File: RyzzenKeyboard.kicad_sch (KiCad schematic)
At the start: 16 parts, among them SW1 SW_SPDT, U100 STM32F411CEUx, Y1 25MHz

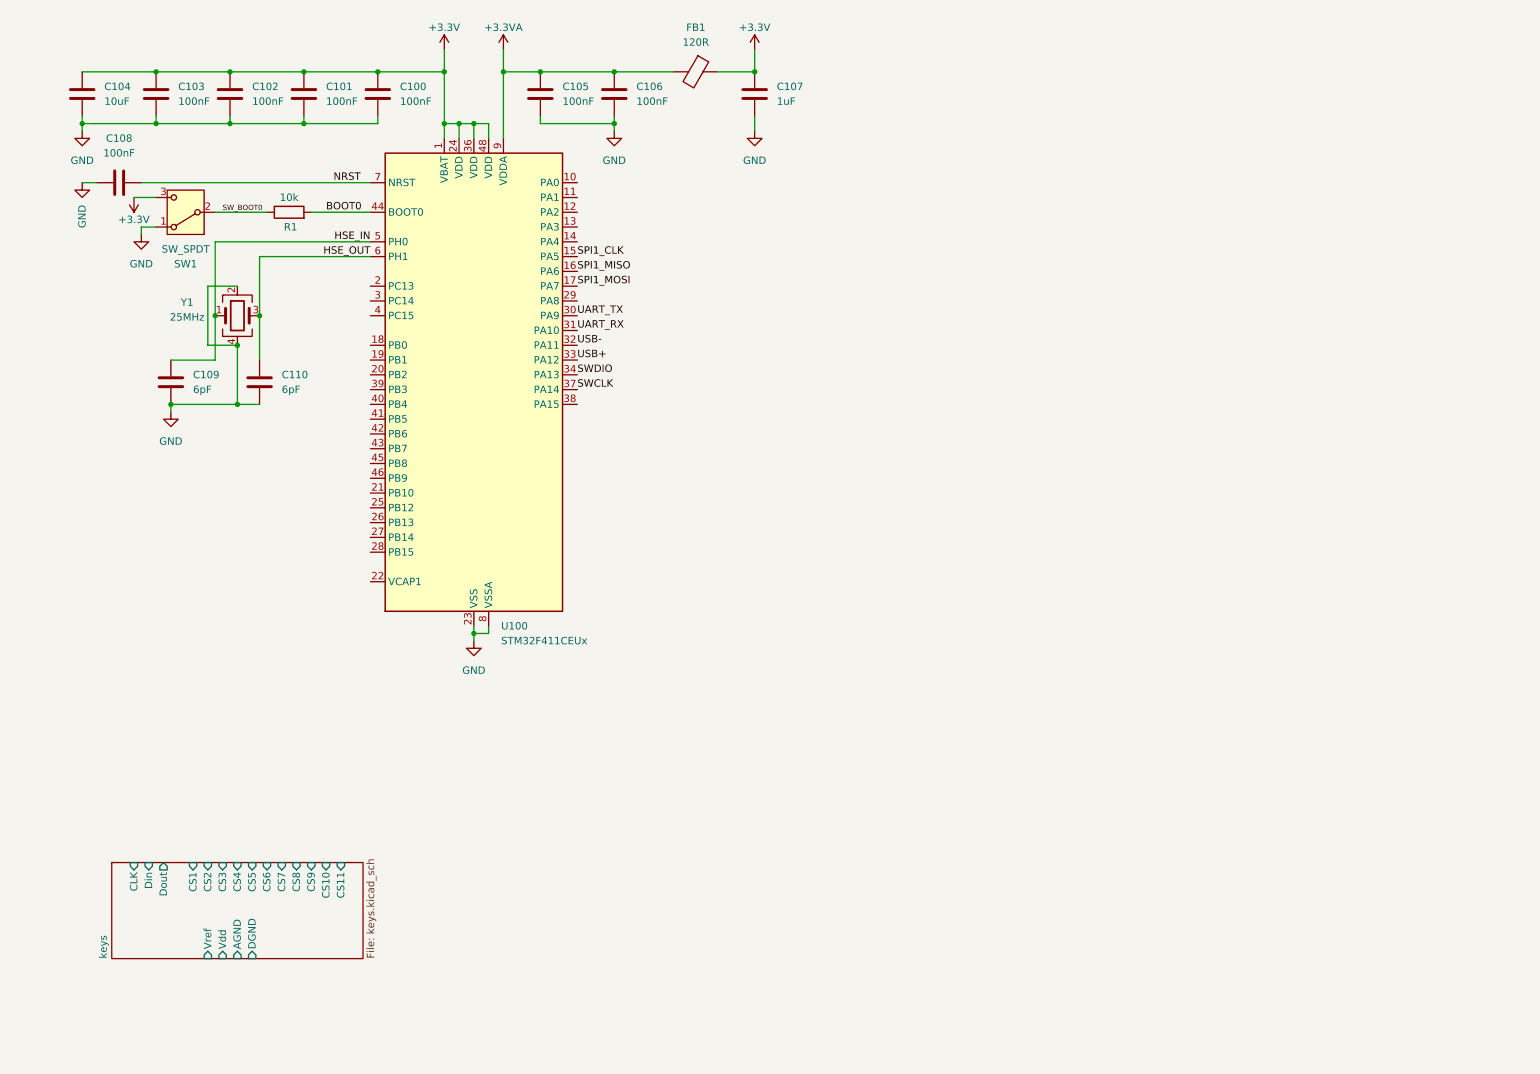
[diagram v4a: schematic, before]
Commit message: [UPDATE](TMR) switched to TMR sensors + added ldo
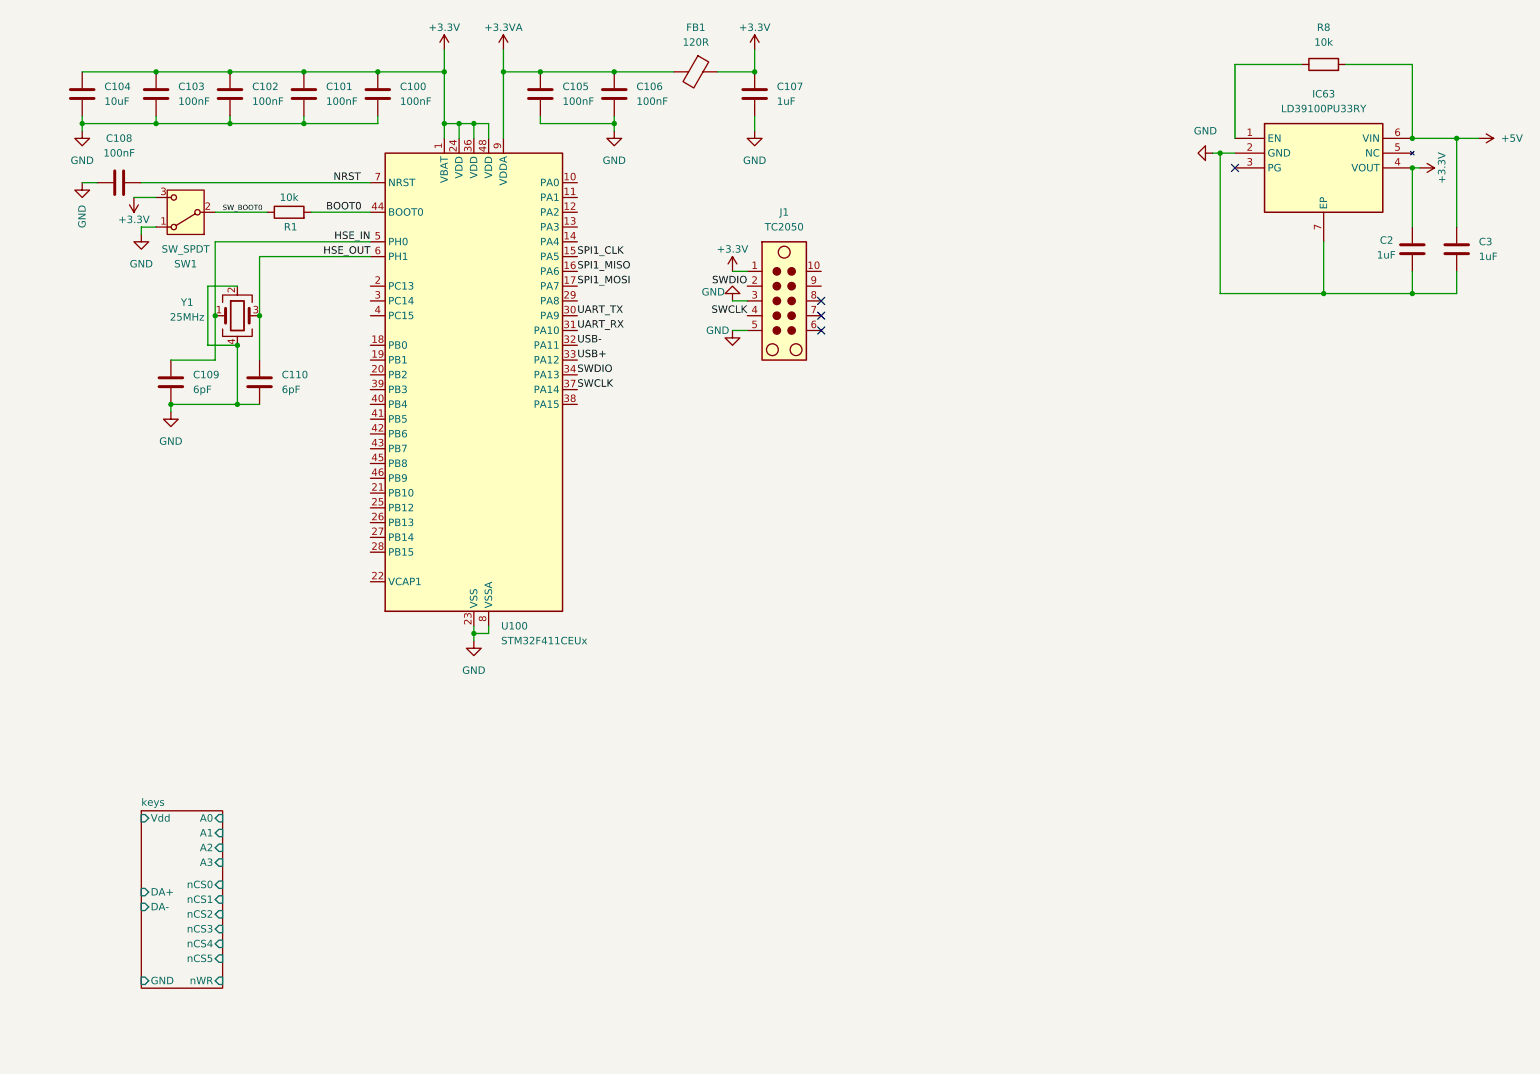
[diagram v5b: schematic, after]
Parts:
- added C2, C3: 1uF, symbol Device:C
- added IC63: LD39100PU33RY, SON95P300X300X90-7N-D, symbol LD39100PU33RY:LD39100PU33RY
- added J1: TC2050, Connector:Tag-Connect_TC2050-IDC-NL_2x05_P1.27mm_Vertical, symbol Connector:TC2050
- added R8: 10k, symbol Device:R
- Y1: footprint (none) -> ECS-250-8-30B-CKM:XTAL_ECS-250-8-30B-CKM
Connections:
- net +3.3V: now also C2.1, IC63.4 (VOUT), J1.1
- net GND: now also C2.2, C3.2, IC63.2 (GND), IC63.7 (EP), J1.3, J1.5
- net SWCLK: now also J1.4
- net SWDIO: now also J1.2
- new net: IC63.1 (EN), R8.1
- new net +5V: C3.1, IC63.6 (VIN), R8.2
- no-connect marks 0 -> 4
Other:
- sheet keys ports: added A0, A1, A2, A3, DA+, DA-, GND, nCS0, nCS1, nCS2, nCS3, nCS4, nCS5, nWR; removed AGND, CLK, CS1, CS10, CS11, CS2, CS3, CS4, CS5, CS6, CS7, CS8, CS9, DGND, Din, Dout, Vref

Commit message: [ADD](HID SPI Bridge)
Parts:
- removed SW1: SW_SPDT, symbol Switch:SW_SPDT
- added D1: LED, symbol Device:LED
- added R9: 1k5, symbol Device:R
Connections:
- net SW_BOOT0 is gone; now on net GND: R1.1
- net GND: now also R9.2
- net at IC63.3 (PG): now also D1.2 (A)
- net +5V renamed VBUS
- new net: D1.1 (K), R9.1
- no-connect marks 4 -> 3
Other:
- added sheet HID_SPI_bridge (HID_SPI_bridge.kicad_sch)
- moved on the sheet: C2, C3, IC63, R8

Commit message: [ADD](General) v1
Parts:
- removed R9: 1k5, symbol Device:R
- added R3: 1k5, symbol Device:R
- renumbered C104 to C1, C106 to C10, C107 to C11, C2 to C12, C3 to C13, C103 to C2, C109 to C3, C108 to C4, C102 to C5, C110 to C6, C101 to C7, C100 to C8, C105 to C9, IC63 to IC1, R8 to R2, U100 to U1
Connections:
- net +3.3V: now also D1.2 (A)
- net GND: now also J1.9, R3.2
- net NRST: now also J1.10
- net UART_RX: now also J1.7
- net UART_TX: now also J1.8
- net at IC1.3 (PG): no longer D1.2 (A)
- net at D1.1 (K): now also R3.1
- net DA+: now reaches U1.10 (PA0)
- net DA-: now reaches U1.11 (PA1)
- net nWR: now reaches U1.13 (PA3)
- net A0: now reaches U1.18 (PB0)
- net A1: now reaches U1.19 (PB1)
- net A2: now reaches U1.20 (PB2)
- net A3: now reaches U1.21 (PB10)
- net CS_USB3: now reaches U1.25 (PB12)
- net CS_USB2: now reaches U1.26 (PB13)
- net CS_USB1: now reaches U1.27 (PB14)
- net nCS0: now reaches U1.39 (PB3)
- net nCS1: now reaches U1.40 (PB4)
- net nCS2: now reaches U1.41 (PB5)
- net nCS3: now reaches U1.42 (PB6)
- net nCS4: now reaches U1.43 (PB7)
- net nCS5: now reaches U1.45 (PB8)
- net USB+: no longer names the net of U1.33 (PA12)
- net USB-: no longer names the net of U1.32 (PA11)
- no-connect marks 3 -> 14
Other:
- added sheet HID_SPI_bridge1 (HID_SPI_bridge.kicad_sch)
- added sheet HID_SPI_bridge2 (HID_SPI_bridge.kicad_sch)
- sheet HID_SPI_bridge ports: added NRST, SPI_CS, SPI_MISO, SPI_MOSI, SPI_SCK, SWCLK, SWDIO; removed none
- note added: "Analog keys"
- note added: "Main microcontroller"
- note added: "Power supply"
- note added: "SPI to triple USB HID bridge"
- company: (none) -> Ryzzen
- title: (none) -> TMR based triple USB Keyboard
- moved on the sheet: C1, C10, C11, C12, C13, C2, C3, C4, C5, C6, C7, C8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

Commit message: [ADD](General) v2 split
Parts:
- added D37: D_Schottky, symbol Device:D_Schottky
- added J2, J3: Conn_01x16_Socket, symbol Connector:Conn_01x16_Socket
- added J4: USB_C_Receptacle_USB2.0_14P, symbol Connector:USB_C_Receptacle_USB2.0_14P
- added R10, R11: 5.1k, symbol Device:R
- added R4: 10k, symbol Device:R
- added U37: W25Q32JVSS, Package_SO:SOIC-8_5.3x5.3mm_P1.27mm, symbol Memory_Flash:W25Q32JVSS
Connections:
- net +3.3V: now also R4.1, U37.8 (VCC)
- net +3.3VA: now also J2.14 (Pin_14), J3.14 (Pin_14)
- net A0: now also J2.6 (Pin_6), J3.6 (Pin_6)
- net A1: now also J2.5 (Pin_5), J3.5 (Pin_5)
- net A2: now also J2.4 (Pin_4), J3.4 (Pin_4)
- net A3: now also J2.3 (Pin_3), J3.3 (Pin_3)
- net DA+: now also J2.12 (Pin_12), J3.12 (Pin_12)
- net DA-: now also J2.11 (Pin_11), J3.11 (Pin_11)
- net GND: now also J2.1 (Pin_1), J2.10 (Pin_10), J2.13 (Pin_13), J2.16 (Pin_16), J3.1 (Pin_1), J3.10 (Pin_10), J3.13 (Pin_13), J3.16 (Pin_16), J4.A1 (GND), J4.A12 (GND), J4.B1 (GND), J4.B12 (GND), R10.1, R11.1, U37.4 (GND)
- net SPI1_CLK: now also U37.6 (CLK)
- net SPI1_MISO: now also U37.2 (DO/IO_{1})
- net SPI1_MOSI: now also U37.5 (DI/IO_{0})
- net VBUS: now also D37.1 (K), J2.15 (Pin_15), J3.15 (Pin_15)
- net nCS0: now also J2.8 (Pin_8), J3.8 (Pin_8)
- net nCS1: now also J2.7 (Pin_7), J3.7 (Pin_7)
- net nWR: now also J2.9 (Pin_9), J3.9 (Pin_9)
- net nCS_FLASH: now reaches U1.28 (PB15)
- net nCS_FLASH: now also U37.1 (~{CS})
- net Din: now reaches U1.46 (PB9)
- net Din: now also J2.2 (Pin_2), J3.2 (Pin_2)
- new net: D37.2 (A), J4.A4 (VBUS), J4.A9 (VBUS), J4.B4 (VBUS), J4.B9 (VBUS)
- new net: R4.2, U37.3 (~{WP}/IO_{2}), U37.7 (~{HOLD}/~{RESET}/IO_{3})
- new net: J4.A5 (CC1), R10.2
- new net: J4.B5 (CC2), R11.2
- new net USB+: J4.A6 (D+), J4.B6 (D+)
- new net USB-: J4.A7 (D-), J4.B7 (D-)
- no-connect marks 14 -> 13
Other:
- added sheet LEDs (leds.kicad_sch)
- sheet keys ports: added none; removed nCS2, nCS3, nCS4, nCS5
- note added: "Connectors"
- note added: "LEDs"
